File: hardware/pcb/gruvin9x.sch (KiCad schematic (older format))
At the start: 246 parts, among them IC1 ATMEGA2560-A_GRUVIN, J1 JUMPER_2W, J4 JUMPER_2W, K1 CONN_3, K2 CONN_3, K3 CONN_3, K4 CONN_3, K5 CONN_3, K6 CONN_3, P1 CONN_3X2, P10 CONN_5X2, P12 CONN_4, P13 CONN_8, P14 CONN_2, P15 CONN_4, P16 CONN_1, P17 CONN_1, P18 CONN_2, P2 CONN_5, P20 CONN_8, P21 CONN_3, P23 CONN_1, P24 CONN_1, P25 CONN_1, P26 CONN_1, P3 CONN_6, P4 CONN_9, P5 CONN_9, P6 CONN_6, P7 CONN_12, P8 CONN_30_LCD_GRUVIN, P9 CONN_1, Q1 BC847C, Q2 BC847C, Q3 BC857C, Q4 BC847C, Q5 BC847C, Q6 Si2319DS, Q7 BC847C, Q8 BC847C, SW1 SW_PUSH, SW2 SW_PUSH, SW3 SW_PUSH, SW4 SW_PUSH, SW5 SW_PUSH, SW6 SW_PUSH, U1 78L05, U2 78L05, U3 LN-6206-30, U4 TPS77601, U5 REF3012, X1 16MHz

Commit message: Addition of soft off switch to PCB V4.1 This will allow better EEPROM management as the CPU gets to say when the power is switched off, like the DX6i, DX8, Multiplex MC4000 etc.
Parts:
- removed P16, P17: CONN_1, symbol CONN_1
- added C63: 0.1uF, symbol C
- added D2: 5.1v, symbol ZENER
- added D5: DIODESCH, symbol DIODESCH
- added Q10: Si2319DS, symbol MOSFET_P
- added Q9: BC847C, SOT23-BCE, symbol BC847C
- added R103: 1k, symbol R
- added R111, R112, R114: 5K1, symbol R
- added R113: 100K, symbol R
- added R115: 100k, symbol R
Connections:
- net labels added: Jack_Presence
- wire segments 690 -> 707

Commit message: Just renaming a few nets to more sensible names
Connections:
- net labels added: Back_Light_EL_TTL, Hold_PWR_ON, Jack_Presence_TTL, Spare1\LED-BL-opt, Spare2\Vib-opt, Vib-PWM-opt
- net labels removed: Back_Light_TTL, Spare3, Spare4, Spare5, Spare6, VIB_OPTION
- wire segments 707 -> 708
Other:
- moved on the sheet: C63, D2, D5, P23, P24, P9, Q9, R103, R111, R112, R115

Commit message: V4.1 PCB change to allow soft off to be bypassed if it turns out to a duff mod.
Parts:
- added R116: 0R, symbol R
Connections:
- wire segments 708 -> 710
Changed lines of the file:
@@
-EESchema Schematic File Version 2  date 05/10/2011 19:48:52
+EESchema Schematic File Version 2  date 10/10/2011 18:19:23
 LIBS:device
 LIBS:transistors
@@
 Sheet 1 1
 Title "Main Controller PCB for 100pin ATMega"
-Date "5 oct 2011"
+Date "10 oct 2011"
 Rev "4.1"
 Comp ""
@@
 Comment4 "Licensed under the TAPR Open Hardware License (see file,  LICENSE)"
 $EndDescr
+Connection ~ 18350 8850
+Wire Wire Line
+	18350 9800 18350 8850
 Wire Wire Line
 	12350 14900 11350 14900
@@
 	9000 13850 10600 13850
 Wire Wire Line
-	20250 13700 20250 13650
+	20250 13650 20250 13700
 Connection ~ 21050 14200
 Wire Wire Line
@@
 	4650 12650 6400 12650
 Wire Wire Line
-	15350 4800 15700 4800
+	15700 4800 15350 4800
 Wire Wire Line
 	14250 4900 13700 4900
@@
 	19500 12550 19300 12550
 Wire Wire Line
-	20300 11900 20300 12250
+	20300 12250 20300 11900
 Connection ~ 20900 12650
 Wire Wire Line
@@
 Connection ~ 1550 3150
 Wire Wire Line
-	1550 2550 1700 2550
+	1700 2550 1550 2550
 Connection ~ 1550 2550
 Wire Wire Line
@@
 	13250 14900 13250 14750
 Wire Wire Line
-	13250 14300 13250 14350
+	13250 14350 13250 14300
 Connection ~ 16700 14300
 Wire Wire Line
@@
 	17100 14300 15150 14300
 Wire Wire Line
-	17100 15450 17100 14550
+	17100 14550 17100 15450
 Wire Wire Line
 	15550 14850 15550 14600
@@
 Connection ~ 7450 7900
 Wire Wire Line
-	6000 9750 6000 9650
+	6000 9650 6000 9750
 Wire Wire Line
 	10050 11550 10650 11550
@@
 Connection ~ 14100 3050
 Wire Wire Line
-	11500 4800 11500 5100
+	11500 5100 11500 4800
 Wire Wire Line
 	11500 4800 10000 4800
@@
 	10200 3950 10200 4250
 Wire Wire Line
-	10950 4400 10950 4350
+	10950 4350 10950 4400
 Wire Wire Line
 	10950 4400 10650 4400
@@
 Connection ~ 18150 7550
 Wire Wire Line
-	18850 7550 18150 7550
+	18150 7550 18850 7550
 Wire Wire Line
 	18850 7550 18850 7400
@@
 	18850 7400 19050 7400
 Wire Wire Line
-	18150 7850 18100 7850
+	18100 7850 18150 7850
 Wire Wire Line
 	18150 7850 18150 8050
@@
 	18150 8050 18100 8050
 Wire Wire Line
-	17450 7450 17600 7450
+	17600 7450 17450 7450
 Wire Wire Line
 	17600 8050 17450 8050
@@
 Connection ~ 4800 2900
 Wire Wire Line
-	5150 2900 4800 2900
+	4800 2900 5150 2900
 Wire Wire Line
 	5150 2900 5150 2800
@@
 	6000 9650 6400 9650
 Wire Wire Line
-	5000 9150 5100 9150
+	5100 9150 5000 9150
 Wire Wire Line
 	4800 9450 5000 9450
 Connection ~ 5700 9750
 Wire Wire Line
-	5500 9750 6000 9750
-Wire Wire Line
-	6000 9150 6000 9350
+	6000 9750 5500 9750
+Wire Wire Line
+	6000 9350 6000 9150
 Wire Wire Line
 	6000 9350 6400 9350
@@
 	14100 2900 15100 2900
 Wire Wire Line
-	14100 2400 14550 2400
+	14550 2400 14100 2400
 Wire Wire Line
 	14100 2750 14550 2750
@@
 Connection ~ 6000 8500
 Wire Wire Line
-	5500 9150 6000 9150
+	6000 9150 5500 9150
 Connection ~ 5700 9150
 Wire Wire Line
@@
 	5750 4600 6300 4600
 Wire Wire Line
-	4850 3850 5000 3850
-Wire Wire Line
-	4850 5050 4850 3850
+	5000 3850 4850 3850
+Wire Wire Line
+	4850 3850 4850 5050
 Wire Wire Line
 	5100 11450 4450 11450
@@
 	19050 7200 18450 7200
 Wire Wire Line
-	18000 7300 18450 7300
+	18450 7300 18000 7300
 Wire Wire Line
 	18000 7300 18000 6900
@@
 	18050 6300 17700 6300
 Wire Wire Line
-	18450 6400 18500 6400
+	18500 6400 18450 6400
 Wire Wire Line
 	18450 6400 18450 6600
@@
 Connection ~ 17550 7650
 Wire Wire Line
-	18150 7650 18100 7650
+	18100 7650 18150 7650
 Wire Wire Line
 	18150 7650 18150 7450
@@
 	18950 10650 19100 10650
 Wire Wire Line
-	18850 11050 19100 11050
+	19100 11050 18850 11050
 Wire Wire Line
 	18850 11050 18850 9050
@@
 Connection ~ 17250 7650
 Wire Wire Line
-	17450 8250 17450 7450
+	17450 7450 17450 8250
 Connection ~ 17450 8050
 Wire Wire Line
@@
 	9000 12950 9500 12950
 Wire Wire Line
-	13850 9850 13900 9850
+	13900 9850 13850 9850
 Wire Wire Line
 	14900 10200 14900 10050
@@
 Connection ~ 7850 8550
 Wire Wire Line
-	6000 7900 6000 7950
-Wire Wire Line
-	7850 7900 6000 7900
+	6000 7950 6000 7900
+Wire Wire Line
+	6000 7900 7850 7900
 Connection ~ 7550 7900
 Wire Wire Line
@@
 	15800 14850 15800 14950
 Wire Wire Line
-	15800 15450 17100 15450
+	17100 15450 15800 15450
 Wire Wire Line
 	16700 15450 16700 14850
@@
 	13250 14750 13550 14750
 Wire Wire Line
-	13800 11600 14050 11600
-Wire Wire Line
-	13800 13000 14050 13000
+	14050 11600 13800 11600
+Wire Wire Line
+	14050 13000 13800 13000
 Wire Wire Line
 	17150 11650 17150 12650
@@
 	14950 13200 14950 13250
 Wire Wire Line
-	13800 11600 13800 13000
+	13800 13000 13800 11600
 Wire Wire Line
 	14550 11600 14550 11750
@@
 	13050 10550 13050 10650
 Wire Wire Line
-	16600 10000 16450 10000
-Wire Wire Line
-	16600 9400 16600 10000
+	16450 10000 16600 10000
+Wire Wire Line
+	16600 10000 16600 9400
 Connection ~ 16600 9750
 Wire Wire Line
@@
 	14100 2550 15100 2550
 Wire Wire Line
-	14100 3400 14100 2400
+	14100 2400 14100 3400
 Connection ~ 14100 3200
 Wire Wire Line
@@
 	6400 11950 5550 11950
 Wire Wire Line
-	1550 3450 1550 2550
+	1550 2550 1550 3450
 Wire Wire Line
 	6400 12150 5550 12150
@@
 	18800 12550 18800 12250
 Wire Wire Line
-	22150 12650 22150 12350
+	22150 12350 22150 12650
 Wire Wire Line
 	18350 12250 19300 12250
@@
 Connection ~ 14900 4900
 Wire Wire Line
-	15350 5050 15350 4800
+	15350 4800 15350 5050
 Connection ~ 15350 4900
 Wire Wire Line
@@
 	10250 14500 10250 14400
 Wire Wire Line
-	20650 13700 20250 13700
+	20250 13700 20650 13700
 Wire Wire Line
 	20450 14200 21050 14200
@@
 Connection ~ 20300 12250
 Wire Wire Line
-	20300 12650 22150 12650
+	22150 12650 20300 12650
 Connection ~ 21350 12650
 Wire Wire Line
@@
 	10150 10350 10650 10350
 Wire Wire Line
-	22050 9550 22150 9550
+	22150 9550 22050 9550
 Connection ~ 21150 8400
 Wire Wire Line
@@
 	21550 10700 21550 10200
 Wire Wire Line
-	22050 10800 22050 9550
+	22050 9550 22050 10800
+Wire Wire Line
+	18350 10300 18350 10950
+Connection ~ 18350 10950
+$Comp
+L R R116
+U 1 1 4E9328F9
+P 18350 10050
+F 0 "R116" V 18430 10050 50  0000 C CNN
+F 1 "0R" V 18350 10050 50  0000 C CNN
+	1    18350 10050
+	1    0    0    -1
+$EndComp
 $Comp
 L GND #PWR01

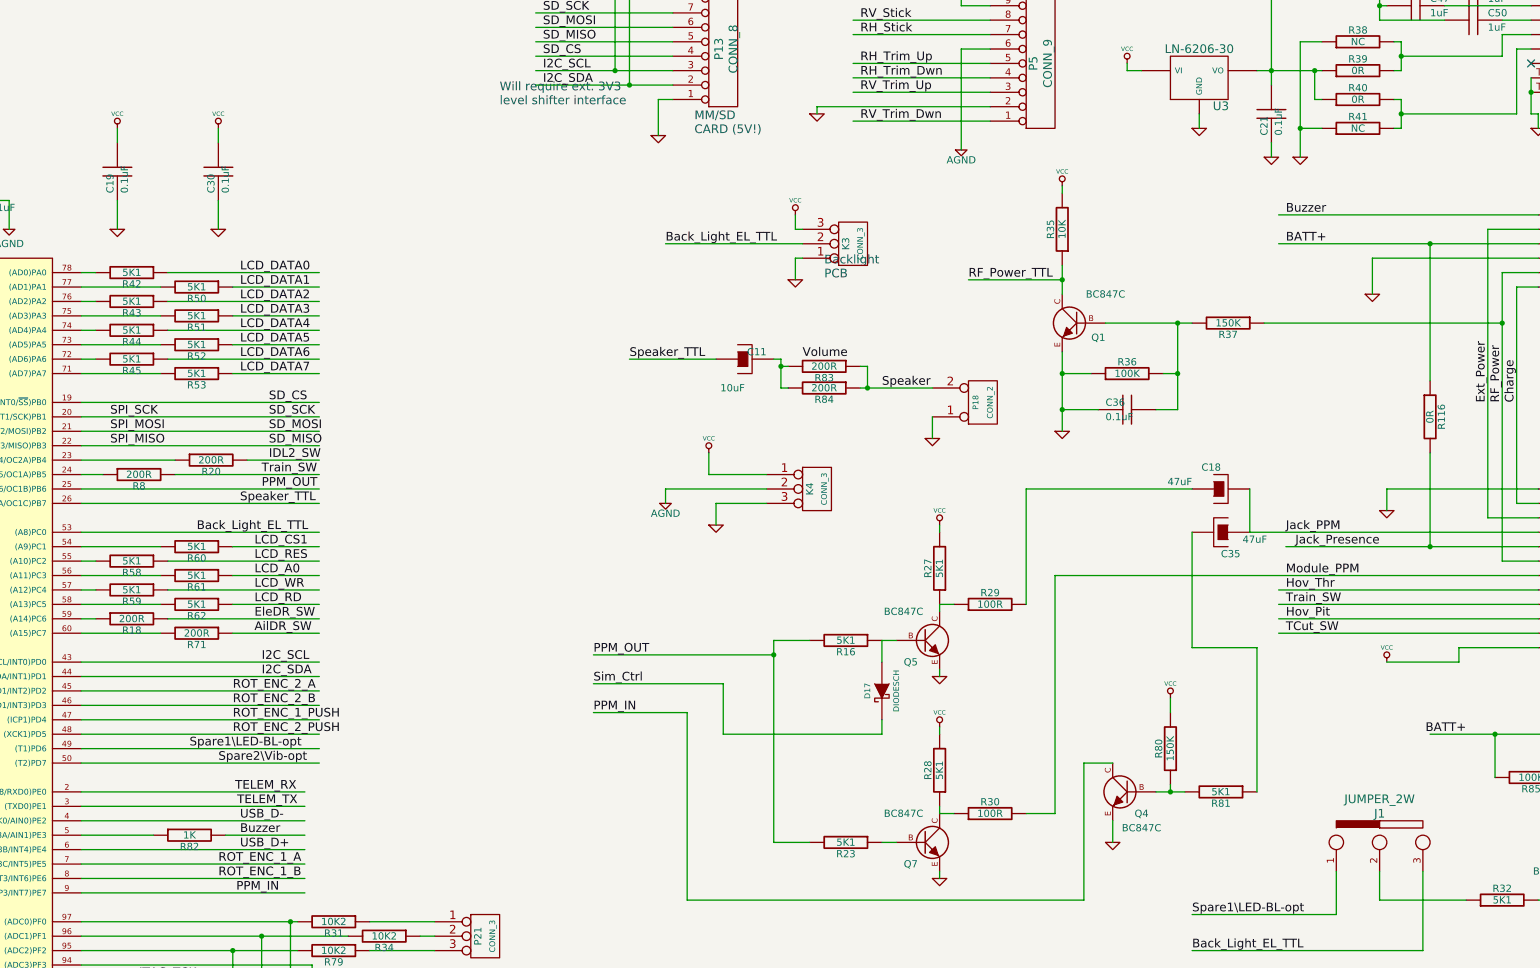
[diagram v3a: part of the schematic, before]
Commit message: A couple of small changes to V4.1, mainly track thickening, and silkscreen tidy. Going to do one last via check then we are done. Have double and triple checked the changes from V4.0 and they all look good.
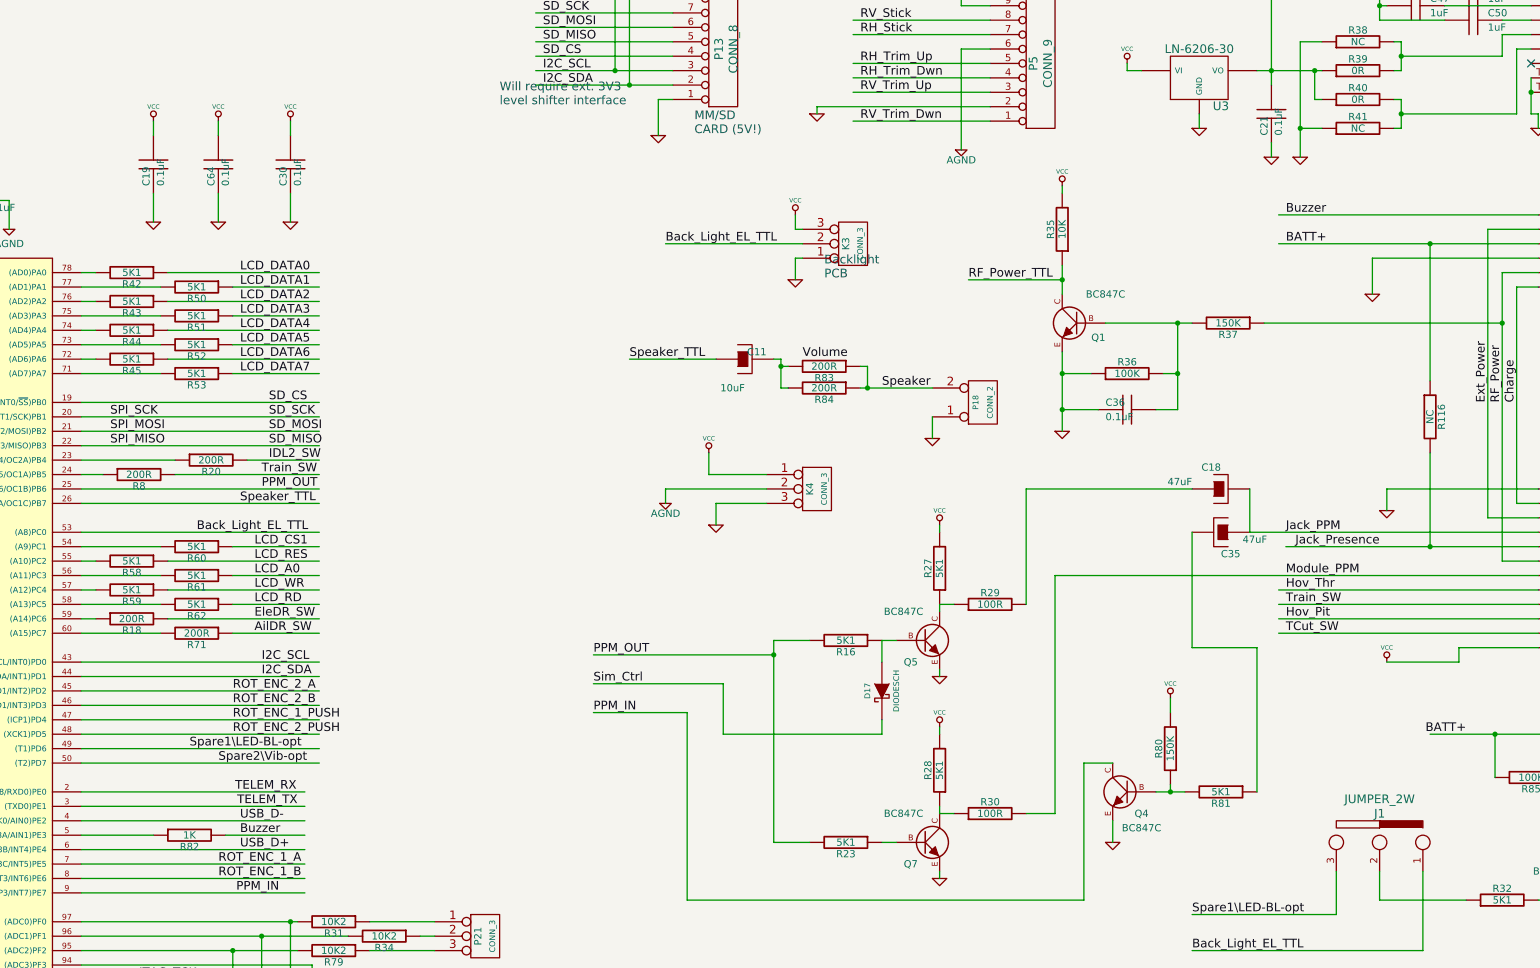
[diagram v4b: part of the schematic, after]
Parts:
- added C64: 0.1uF, symbol C
- R116: value 0R -> NC
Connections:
- wire segments 710 -> 712
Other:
- moved on the sheet: C19, C30

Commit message: Potential V4.1 changes for Bryan to check out.
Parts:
- removed K4: CONN_3, symbol CONN_3
- added K4: CONN_5, symbol CONN_5
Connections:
- net labels added: BATT+_FUSED
- wire segments 712 -> 717
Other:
- moved on the sheet: F1
